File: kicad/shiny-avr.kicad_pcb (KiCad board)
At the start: 4 copper layers, 54.4 x 20.3 mm, 39 parts, among them J1 USB_B_Micro, J2 SWD, U1 AMS1117-3.3, U2 STM32F103C6Tx, U3 ATtiny85-20PU, U4 ATtiny85-20PU, Y1 8 MHz

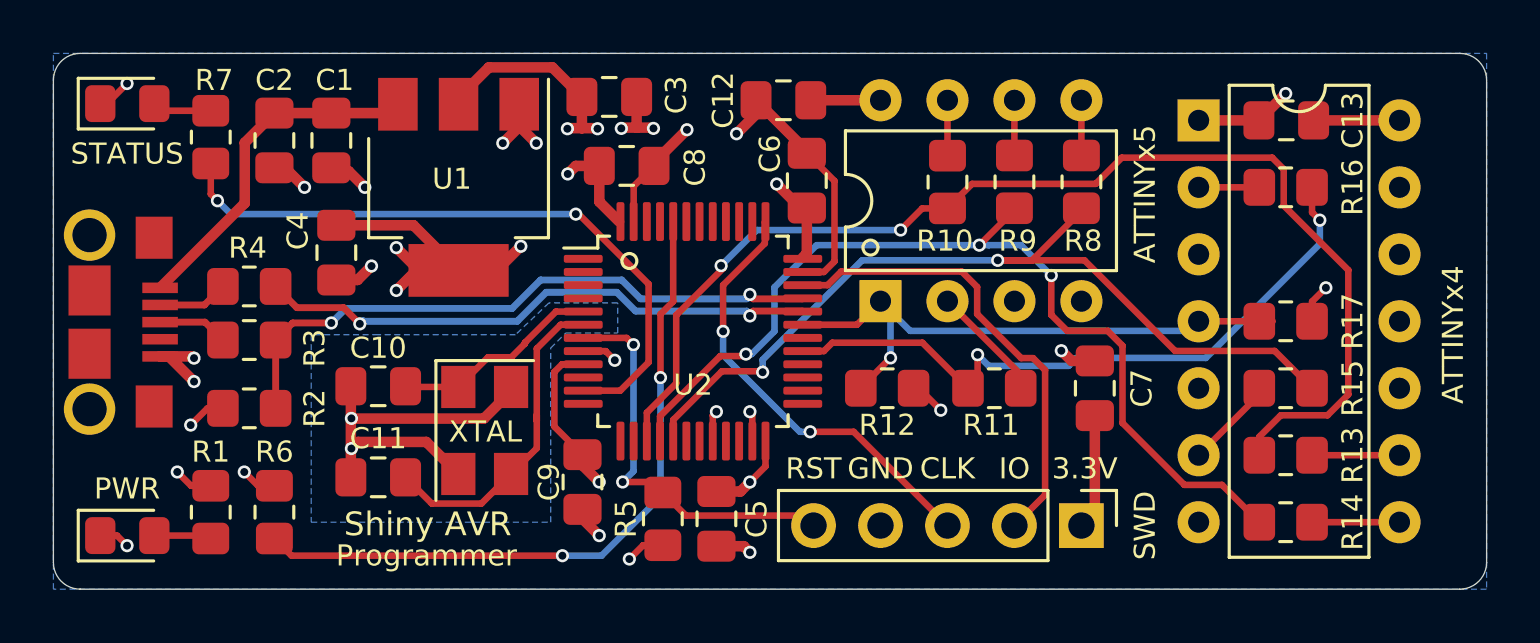
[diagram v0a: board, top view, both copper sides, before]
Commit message: fix: Swapped pins 6 and 7 on ATtinyX4 socket
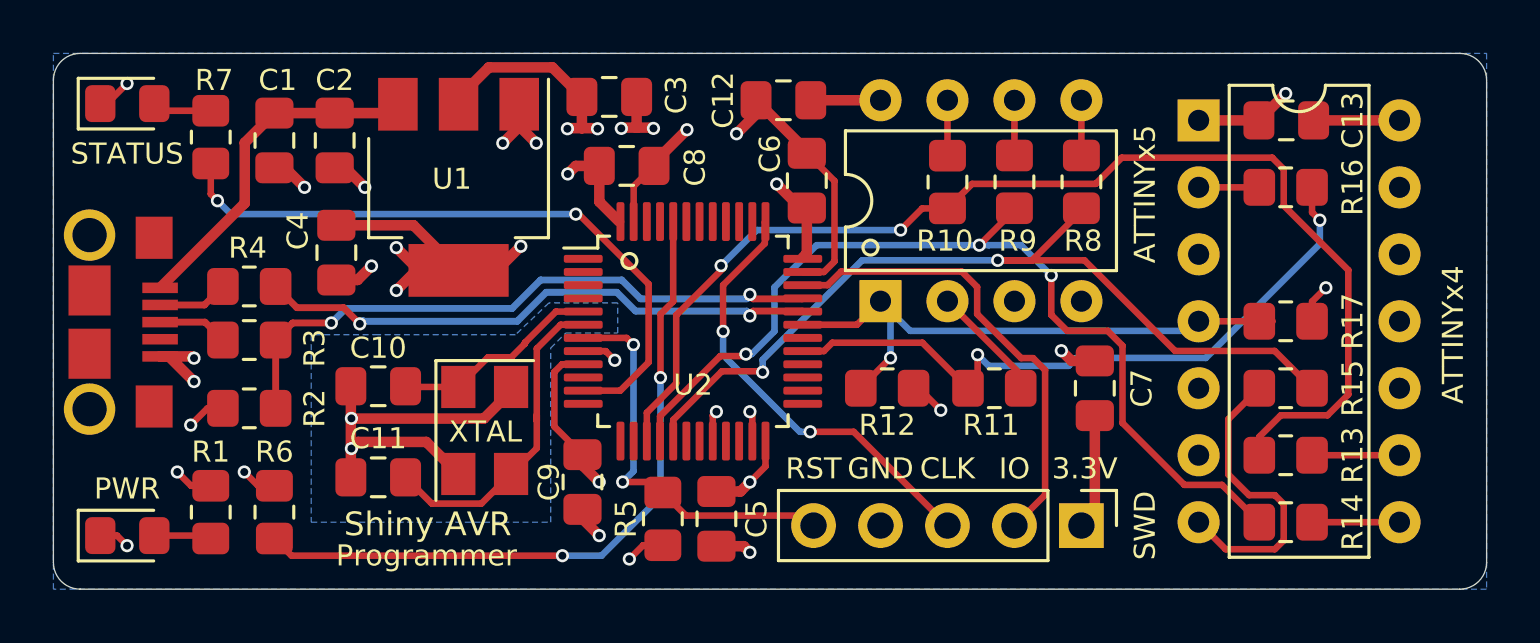
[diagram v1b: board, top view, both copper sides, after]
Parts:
- moved C2 2.29 mm to (140.7, 99.8)
- moved C1 2.16 mm to (138.4, 99.8)
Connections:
- U4 pad 6: Net-(R15-Pad2) -> (no net)
- U4 pad 7: (no net) -> Net-(R15-Pad2)
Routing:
- net Net-(R15-Pad2): track 3.49 -> 11.5 mm
